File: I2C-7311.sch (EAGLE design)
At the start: 47 parts, among them IC1 MAX7311, J1 CONNECTOR-I2CLEFT, J2 CONNECTOR-I2CLEFT, J5 CONNECTOR-GROVE-4P-2.0-347013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, J8 CONNECTOR-GROVE-4P-2.0-347013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, SW1 A0, SW2 A1, SW3 A2

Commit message: 3.0 - new IOB design
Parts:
- removed CON1: (no value), SPCoast:CONNECTOR-DC-POWER-RA
- removed FID3: FIDUCIAL, SPCoast:FIDUCIAL
- removed J5, J8: CONNECTOR-GROVE-4P-2.0-3470130P1, SPCoast:CONNECTOR-GROVE-4P-2.0-3470130P1
- removed R2, R3: 10k, SPCoast:R0603-RES
- added LED1, LED10, LED11, LED12, LED13, LED14, LED15, LED17, LED2, LED3, LED4, LED5, LED6, LED7, LED8, LED9: Y, SPCoast:LED0603-LED
- added PWR: (no value), SPCoast:CONNECTOR-DC-POWER-RA
- added Q0, Q1, Q10, Q11, Q12, Q13, Q14, Q15, Q2, Q3, Q4, Q5, Q6, Q7, Q8, Q9: P-FET, SPCoast:MOSFET-P-044021001
- added R21, R22: 2K0, SPCoast:R0805-RES
- added VIN: 9-12VDC, SPCoast:DOC-POWER_LABEL
- added VIN1, VIN2: CONNECTOR-POWER-L, SPCoast:CONNECTOR-POWER-L
- BOARD1: value (none) -> BOARD80X100-IOB; device SPCoast:BOARD80X100-NOHOLES -> SPCoast:BOARD80X100-IOB
- IC1: device SPCoast:MAX73XX-12AUG -> SPCoast:MAX73XX/AUG
- IOB1, IOB2, IOB3, IOB4: value IO4-IOBBARE -> CONNECTOR-IO4-IOBBARE; device SPCoast:IO4-IOBBARE -> SPCoast:CONNECTOR-IO4-IOBBARE
- J1, J2: value CONNECTOR-I2CLEFT -> (none)
- R1, R10, R11, R12, R13, R14, R15, R16, R4, R5, R6, R7, R8, R9: value 10k -> 2K0; device SPCoast:R0603-RES -> SPCoast:R0805-RES
- SW1, SW2, SW3: device special:SW_DIP-4 -> SPCoast:SW_DIP-4
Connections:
- new net N$10: Q8.D, R15.2
- new net N$11: Q9.D, R12.2
- new net N$12: Q10.D, R13.2
- new net N$13: Q11.D, R14.2
- new net N$14: LED12.A, R15.1
- new net N$15: LED9.A, R12.1
- new net N$2: Q4.D, R11.2
- new net N$23: LED10.A, R13.1
- new net N$24: LED11.A, R14.1
- new net N$28: Q12.D, R22.2
- new net N$29: Q13.D, R16.2
- new net N$3: Q5.D, R8.2
- new net N$30: Q14.D, R1.2
- new net N$31: Q15.D, R21.2
- new net N$32: LED17.A, R22.1
- new net N$33: LED13.A, R16.1
- new net N$34: LED14.A, R1.1
- new net N$35: LED15.A, R21.1
- new net N$4: Q6.D, R9.2
- new net N$44: Q0.D, R7.2
- new net N$45: Q1.D, R4.2
- new net N$46: Q2.D, R5.2
- new net N$47: Q3.D, R6.2
- new net N$48: LED1.A, R7.1
- new net N$49: LED2.A, R4.1
- new net N$5: Q7.D, R10.2
- new net N$50: LED3.A, R5.1
- new net N$51: LED4.A, R6.1
- new net N$6: LED8.A, R11.1
- new net N$7: LED5.A, R8.1
- new net N$8: LED6.A, R9.1
- new net N$9: LED7.A, R10.1
- net +9V: now also PWR.1, VIN1.V+, VIN2.V+; no longer CON1.1, J5.3, J5.4, J8.3, J8.4
- net GND: now also LED1.C, LED10.C, LED11.C, LED12.C, LED13.C, LED14.C, LED15.C, LED17.C, LED2.C, LED3.C, LED4.C, LED5.C, LED6.C, LED7.C, LED8.C, LED9.C, PWR.2, PWR.3, VIN1.GND, VIN2.GND; no longer CON1.2, CON1.3, J5.1, J5.2, J8.1, J8.2
- net P1: now also Q0.G; no longer R1.2
- net P10: now also Q9.G; no longer R10.2
- net P11: now also Q10.G; no longer R11.2
- net P12: now also Q11.G; no longer R12.2
- net P13: now also Q12.G; no longer R13.2
- net P14: now also Q13.G; no longer R14.2
- net P15: now also Q14.G; no longer R15.2
- net P16: now also Q15.G; no longer R16.2
- net P2: now also Q1.G; no longer R2.2
- net P3: now also Q2.G; no longer R3.2
- net P4: now also Q3.G; no longer R4.2
- net P5: now also Q4.G; no longer R5.2
- net P6: now also Q5.G; no longer R6.2
- net P7: now also Q6.G; no longer R7.2
- net P8: now also Q7.G; no longer R8.2
- net P9: now also Q8.G; no longer R9.2
- net VCC: now also Q0.S, Q1.S, Q10.S, Q11.S, Q12.S, Q13.S, Q14.S, Q15.S, Q2.S, Q3.S, Q4.S, Q5.S, Q6.S, Q7.S, Q8.S, Q9.S; no longer R1.1, R10.1, R11.1, R12.1, R13.1, R14.1, R15.1, R16.1, R2.1, R3.1, R4.1, R5.1, R6.1, R7.1, R8.1, R9.1
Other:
- note added: "1.0"
- note added: "3.0"
- note added: "A"
- note added: "Changes IOB v2 - combine Vin/5v and Vout on passthru pins to daughterboard"
- note added: "Feedback LEDs"
- note added: "I2C MAX7311-IOB"
- note added: "MAX7311 - FET drive high/low with 100k builtin pullup"
- note removed: "2.0"
- note removed: "Changes Wrong 7312 footprint (Needs TSSOP24, has QSOP24) power pins for DBs interfered with bottom keep-out moved C4 away from DB"
- note removed: "I2C MAX731x-IOB"
- note removed: "MAX7311 - FET drive high/low with 100k pullup MAX7312 - FET drive high/low MAX7313 - Open Drain output, different footprint"
- note removed: "Pullups needed with MAX7312"

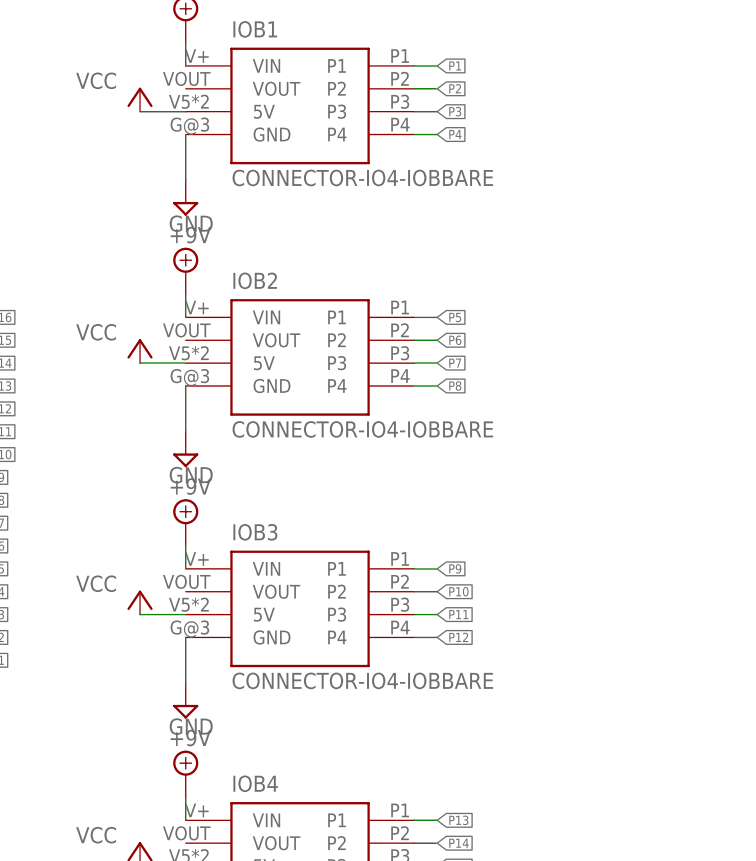
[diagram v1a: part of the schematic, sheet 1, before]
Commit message: updated SPCoast lib for IO4-IOB silkscreen
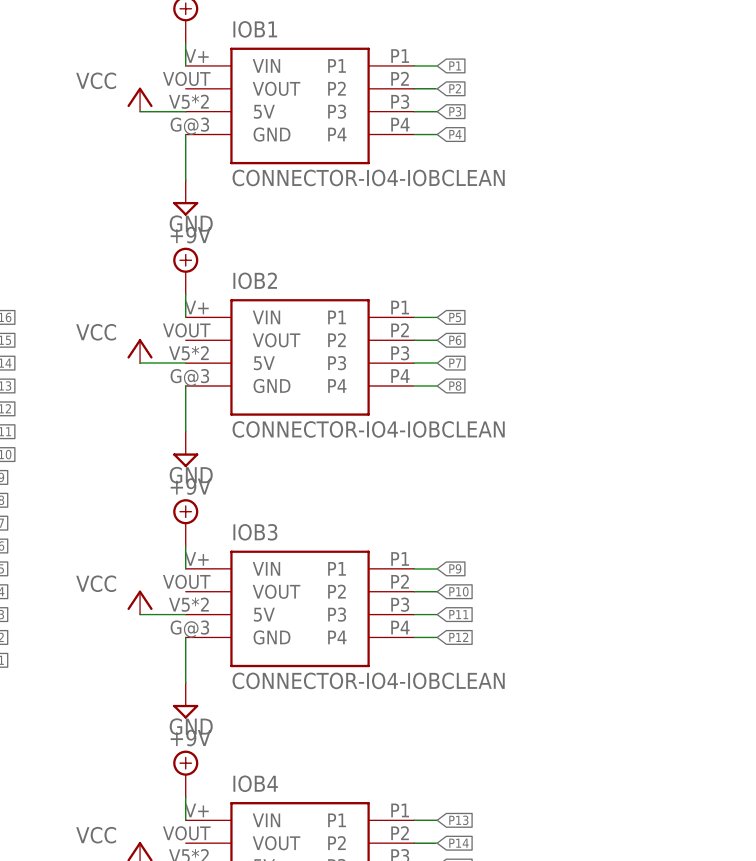
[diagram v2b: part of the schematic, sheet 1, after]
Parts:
- IOB1, IOB2, IOB3: value CONNECTOR-IO4-IOBBARE -> CONNECTOR-IO4-IOBCLEAN; device SPCoast:CONNECTOR-IO4-IOBBARE -> SPCoast:CONNECTOR-IO4-IOBCLEAN
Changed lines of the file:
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@@
 <part name="P+14" library="supply1" deviceset="VCC" device=""/>
 <part name="BOARD1" library="SPCoast" deviceset="BOARD" device="80X100-IOB" value="BOARD80X100-IOB"/>
-<part name="IOB1" library="SPCoast" deviceset="CONNECTOR-IO4-IOB" device="BARE"/>
-<part name="IOB2" library="SPCoast" deviceset="CONNECTOR-IO4-IOB" device="BARE"/>
-<part name="IOB3" library="SPCoast" deviceset="CONNECTOR-IO4-IOB" device="BARE"/>
-<part name="IOB4" library="SPCoast" deviceset="CONNECTOR-IO4-IOB" device="BARE"/>
+<part name="IOB1" library="SPCoast" deviceset="CONNECTOR-IO4-IOB" device="CLEAN" value="CONNECTOR-IO4-IOBCLEAN"/>
+<part name="IOB2" library="SPCoast" deviceset="CONNECTOR-IO4-IOB" device="CLEAN" value="CONNECTOR-IO4-IOBCLEAN"/>
+<part name="IOB3" library="SPCoast" deviceset="CONNECTOR-IO4-IOB" device="CLEAN" value="CONNECTOR-IO4-IOBCLEAN"/>
+<part name="IOB4" library="SPCoast" deviceset="CONNECTOR-IO4-IOB" device="BARE" value="CONNECTOR-IO4-IOBBARE"/>
 <part name="P+3" library="supply1" deviceset="VCC" device=""/>
 <part name="P+7" library="supply1" deviceset="VCC" device=""/>

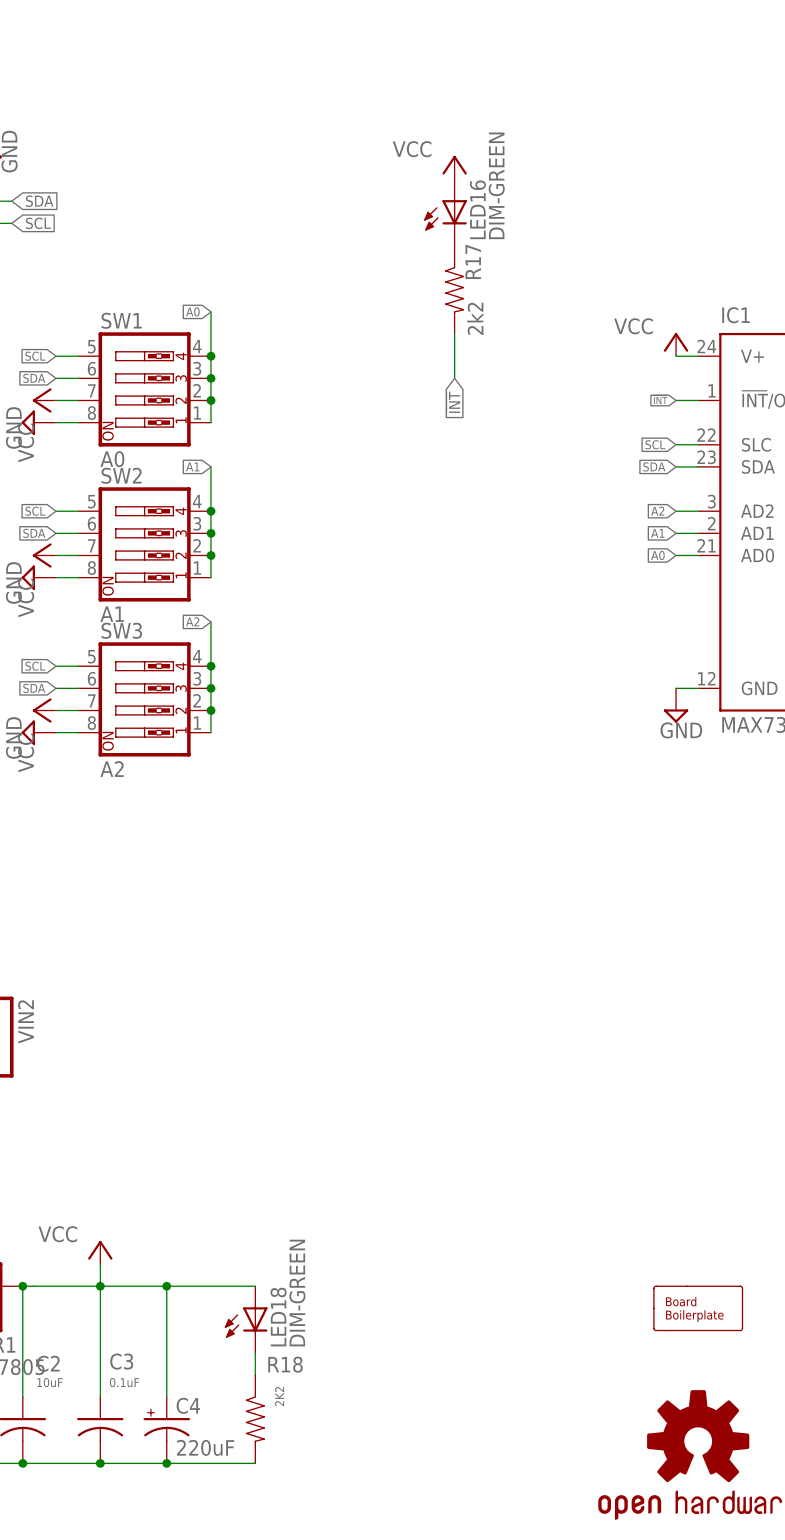
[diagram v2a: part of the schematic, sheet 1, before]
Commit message: updated SPCoast.lbr: LED, VR, C-POL to match reel orientation
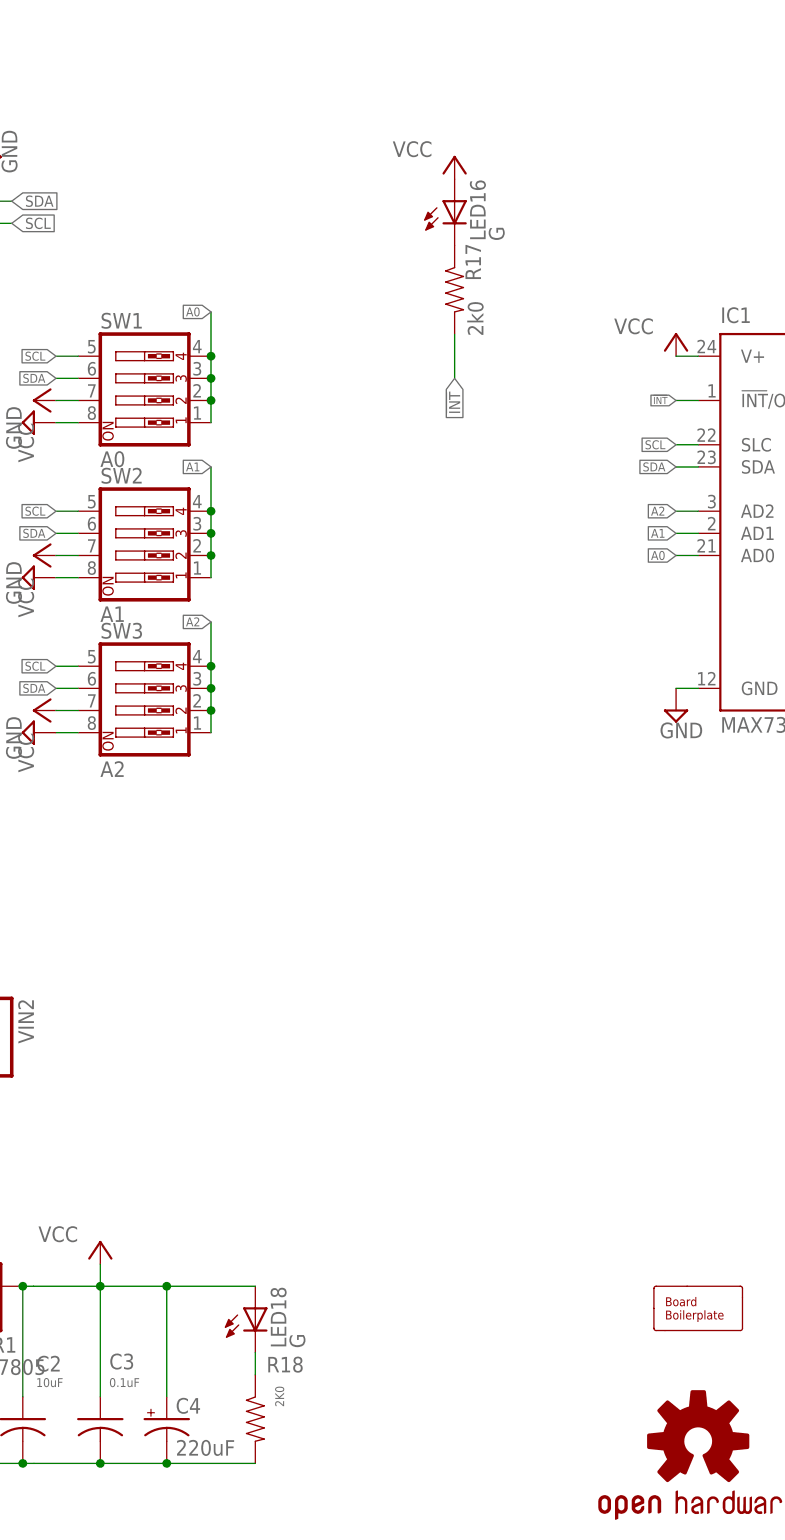
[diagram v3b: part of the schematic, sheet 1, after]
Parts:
- LED16, LED18: value DIM-GREEN -> G
- R17: value 2k2 -> 2k0; device SPCoast:R0603-RES -> SPCoast:R0805-RES
- R18: value 2K2 -> 2K0; device SPCoast:R0603-RES -> SPCoast:R0805-RES
- R19, R20: device SPCoast:R0603-RES -> SPCoast:R0805-RES
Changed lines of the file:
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@@
 <layer number="20" name="Dimension" color="15" fill="1" visible="yes" active="no"/>
 <layer number="21" name="tPlace" color="19" fill="1" visible="yes" active="no"/>
-<layer number="22" name="bPlace" color="17" fill="1" visible="yes" active="no"/>
+<layer number="22" name="bPlace" color="22" fill="1" visible="yes" active="no"/>
 <layer number="23" name="tOrigins" color="30" fill="1" visible="yes" active="no"/>
 <layer number="24" name="bOrigins" color="15" fill="1" visible="yes" active="no"/>
@@
 <layer number="49" name="Reference" color="48" fill="1" visible="yes" active="no"/>
 <layer number="50" name="dxf" color="7" fill="1" visible="yes" active="no"/>
-<layer number="51" name="tDocu" color="24" fill="1" visible="yes" active="no"/>
+<layer number="51" name="tDocu" color="49" fill="1" visible="yes" active="no"/>
 <layer number="52" name="bDocu" color="7" fill="1" visible="yes" active="no"/>
 <layer number="53" name="tGND_GNDA" color="7" fill="9" visible="yes" active="no"/>
@@
 <part name="C2" library="SPCoast" deviceset="CAP*" device="0805" value="10uF"/>
 <part name="P+2" library="supply1" deviceset="VCC" device=""/>
-<part name="R20" library="SPCoast" deviceset="R*" device="0603-RES" value="4k7"/>
-<part name="R19" library="SPCoast" deviceset="R*" device="0603-RES" value="4k7"/>
+<part name="R20" library="SPCoast" deviceset="R*" device="0805-RES" value="4k7"/>
+<part name="R19" library="SPCoast" deviceset="R*" device="0805-RES" value="4k7"/>
 <part name="SCL" library="SPCoast" deviceset="JUMPER-2" device="PTH_LOCK" value="SDA"/>
 <part name="SDA" library="SPCoast" deviceset="JUMPER-2" device="PTH_LOCK" value="SCL"/>
@@
 <part name="VR1" library="SPCoast" deviceset="VREG-?-*" device="DPAK" technology="5" value="CJ7805"/>
 <part name="P+1" library="supply1" deviceset="VCC" device=""/>
-<part name="R18" library="SPCoast" deviceset="R*" device="0603-RES" value="2K2"/>
-<part name="LED18" library="SPCoast" deviceset="LED*" device="0603-LED" value="DIM-GREEN"/>
+<part name="R18" library="SPCoast" deviceset="R*" device="0805-RES" value="2K0"/>
+<part name="LED18" library="SPCoast" deviceset="LED*" device="0603-LED" value="G"/>
 <part name="SUPPLY2" library="supply2" deviceset="+9V" device=""/>
 <part name="V7" library="supply2" deviceset="GND" device=""/>
@@
 <part name="J2" library="SPCoast" deviceset="CONNECTOR-I2C" device="LEFT"/>
 <part name="V12" library="supply2" deviceset="GND" device=""/>
-<part name="R17" library="SPCoast" deviceset="R*" device="0603-RES" value="2k2"/>
-<part name="LED16" library="SPCoast" deviceset="LED*" device="0603-LED" value="DIM-GREEN"/>
+<part name="R17" library="SPCoast" deviceset="R*" device="0805-RES" value="2k0"/>
+<part name="LED16" library="SPCoast" deviceset="LED*" device="0603-LED" value="G"/>
 <part name="P+14" library="supply1" deviceset="VCC" device=""/>
 <part name="BOARD1" library="SPCoast" deviceset="BOARD" device="80X100-IOB" value="BOARD80X100-IOB"/>

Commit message: V3.1
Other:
- note added: "3.1"
- note added: "Changes V3.1 - Fixed SPCoast component orientations on PCB"
- note removed: "3.0"
- note removed: "Changes IOB v2 - combine Vin/5v and Vout on passthru pins to daughterboard"
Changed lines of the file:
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@@
 <text x="152.908" y="23.876" size="2.54" layer="97">IO Expander  with IOB daughterboards</text>
 <text x="152.908" y="6.35" size="3.81" layer="97">John Plocher</text>
-<text x="235.458" y="6.604" size="3.81" layer="97">3.0</text>
+<text x="235.458" y="6.604" size="3.81" layer="97">3.1</text>
 <text x="149.86" y="38.1" size="1.4224" layer="102">Changes
-IOB v2 - combine Vin/5v and Vout on passthru pins to daughterboard</text>
+V3.1 - Fixed SPCoast component orientations on PCB</text>
 <text x="93.98" y="177.8" size="1.778" layer="102">MAX7311 - FET drive high/low with 100k builtin pullup</text>
 </plain>

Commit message: SPCoast lbr footprint update
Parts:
- IOB1, IOB2, IOB3: value CONNECTOR-IO4-IOBCLEAN -> CONNECTOR-IO4-IOBNOBSILK; device SPCoast:CONNECTOR-IO4-IOBCLEAN -> SPCoast:CONNECTOR-IO4-IOBNOBSILK
- IOB4: value CONNECTOR-IO4-IOBBARE -> CONNECTOR-IO4-IOBFULL; device SPCoast:CONNECTOR-IO4-IOBBARE -> SPCoast:CONNECTOR-IO4-IOBFULL
- renumbered FID1 to FID-UL, FID2 to FID-LR
